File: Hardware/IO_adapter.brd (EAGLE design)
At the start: 67.3 x 41.9 mm, 22 parts, among them Y1 32Khz

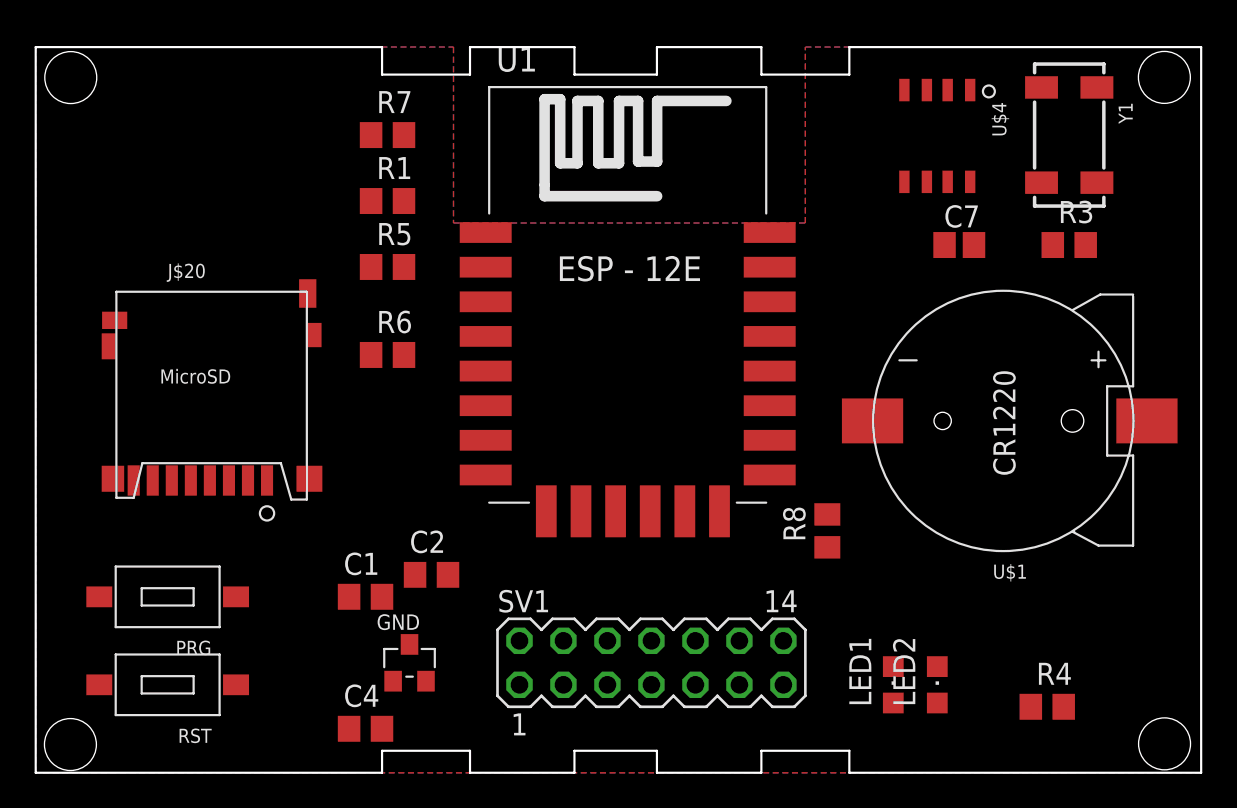
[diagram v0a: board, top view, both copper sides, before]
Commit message: completed routing for both boards
routed out both the base and IO board. Should be ready for verification
There will be errors.
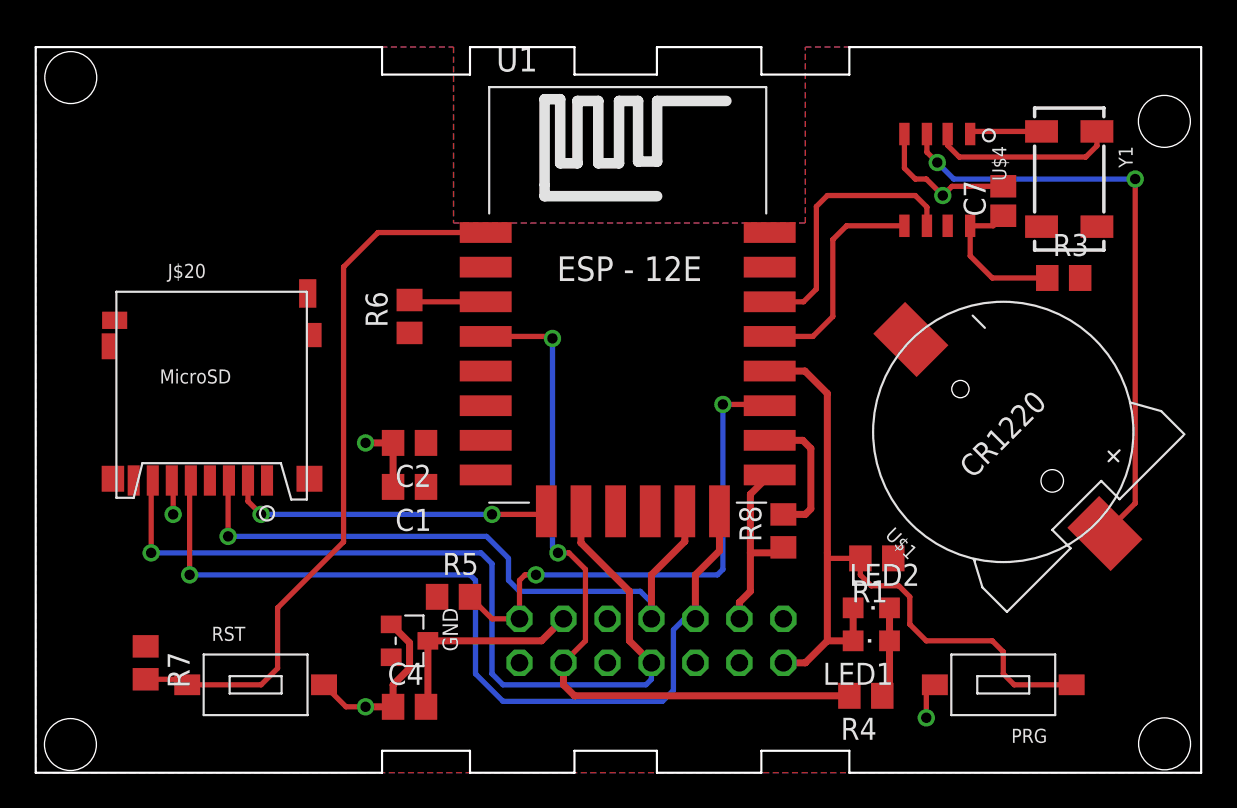
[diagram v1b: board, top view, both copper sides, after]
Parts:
- moved PRG 48.5 mm to (55.9, 5.08)
- moved R1 35.0 mm to (48.6, 12.4), turned to 180 degrees
- moved R7 33.5 mm to (6.35, 6.35), turned to 270 degrees
- moved R5 19.4 mm to (24.1, 10.2)
- moved R4 10.5 mm to (47.9, 4.45), turned to 180 degrees
- moved C2 7.73 mm to (21.6, 19.1), turned to 180 degrees
- moved C1 6.84 mm to (21.6, 16.5), turned to 180 degrees
- moved LED2 5.85 mm to (48.3, 9.53), turned to 270 degrees
- moved RST 5.08 mm to (12.7, 5.08), turned to 0 degrees
- moved C7 3.59 mm to (55.9, 33.0), turned to 90 degrees
- moved LED1 2.84 mm to (48.3, 7.62), turned to 90 degrees
- moved C4 2.84 mm to (21.6, 3.81)
- moved R6 2.56 mm to (21.6, 26.4), turned to 90 degrees
- moved R8 2.54 mm to (43.2, 14.0)
- moved U$4 2.54 mm to (52.1, 34.3)
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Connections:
- removed net ADC10: SV1.2
- removed net GMD: SV1.12
- net 5V: now also SV1.3; no longer SV1.14
- net ADCCS0: now also SV1.1
- net ADCCS1: now also SV1.14; no longer SV1.3
- net CSSD: no longer SV1.10
- net GND: now also SV1.12
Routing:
- net SCLK: track 0.00 -> 51.7 mm, vias 0 -> 1
- net MISO: track 0.00 -> 51.5 mm, vias 0 -> 1
- net ADCCS1: track 0.00 -> 44.3 mm
- net GPIO16: track 0.00 -> 42.4 mm, vias 0 -> 2
- net RST: track 0.00 -> 41.9 mm
- net GND: track 0.00 -> 38.3 mm, vias 0 -> 5
- net MOSI: track 0.00 -> 38.0 mm, vias 0 -> 1
- net VBATT: track 0.00 -> 34.9 mm, vias 0 -> 2
- net ADCCS0: track 0.00 -> 29.9 mm, vias 0 -> 2
- net CSSD: track 0.00 -> 18.8 mm, vias 0 -> 2
- net SCL: track 0.00 -> 15.8 mm
- net SDA: track 0.00 -> 13.0 mm
- net 5V: track 0.00 -> 12.2 mm
- net N$44: track 0.00 -> 10.7 mm
- net N$1: track 0.00 -> 8.87 mm
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
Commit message: added the programming header
I had forgotten the programming header. It's right there now.
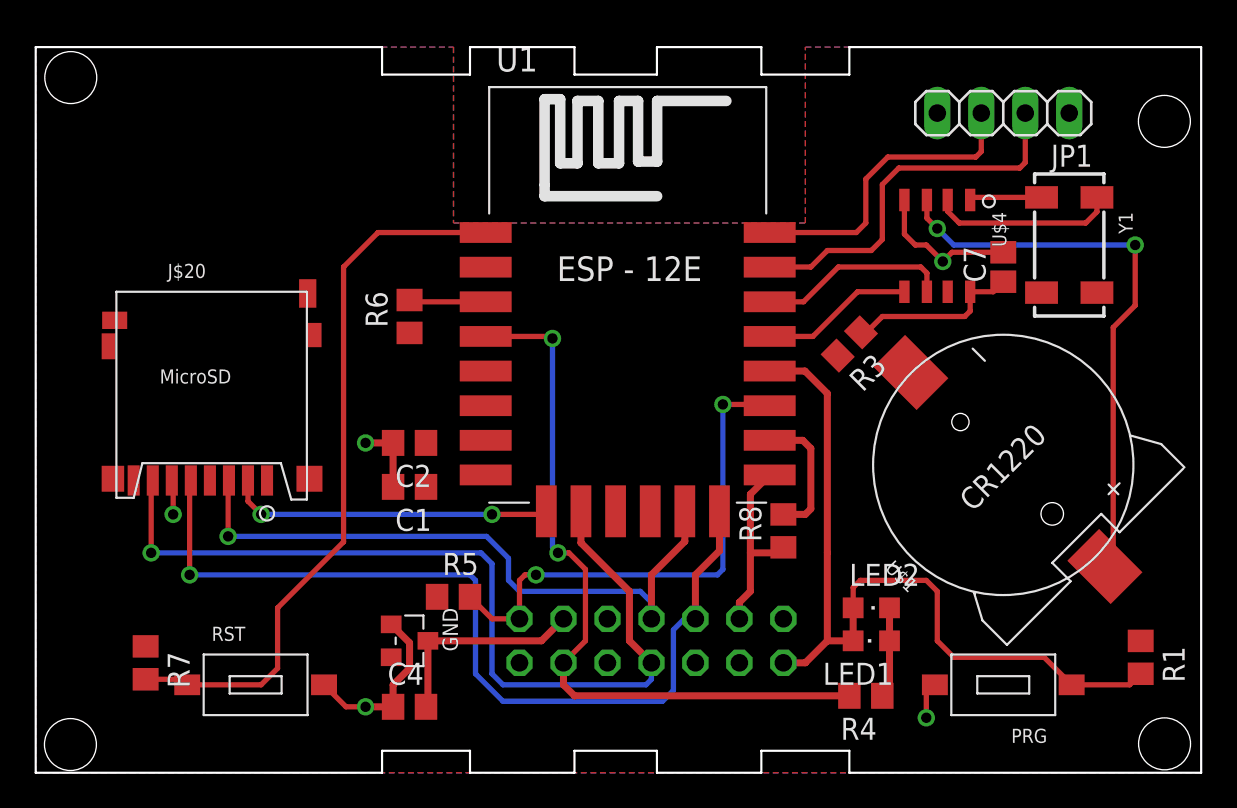
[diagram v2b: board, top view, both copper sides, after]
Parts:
- added JP1: (no value), pinhead:1X04
- moved R1 16.3 mm to (63.8, 6.67), turned to 270 degrees
- moved R3 13.0 mm to (47.0, 24.8), turned to 225 degrees
- moved C7 3.81 mm to (55.9, 29.2)
- moved U$4 3.81 mm to (52.1, 30.5)
- moved Y1 3.81 mm to (59.7, 30.5)
- moved U$1 1.90 mm to (55.9, 17.8)
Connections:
- net 3V3: now also JP1.1
- net GND: now also JP1.4
- net RXD: now also JP1.2
- net TXD: now also JP1.3
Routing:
- net RXD: track 0.00 -> 22.0 mm
- net TXD: track 0.00 -> 17.9 mm
- net SCL: track 15.8 -> 11.1 mm
- net SDA: track 13.0 -> 8.85 mm
- net ADCCS1: track 44.3 -> 47.3 mm
- net VBATT: track 34.9 -> 32.9 mm
- net N$1: track 8.87 -> 10.1 mm

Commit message: moved the MicroSD
now, there is enough room to remove the card in the enclosure
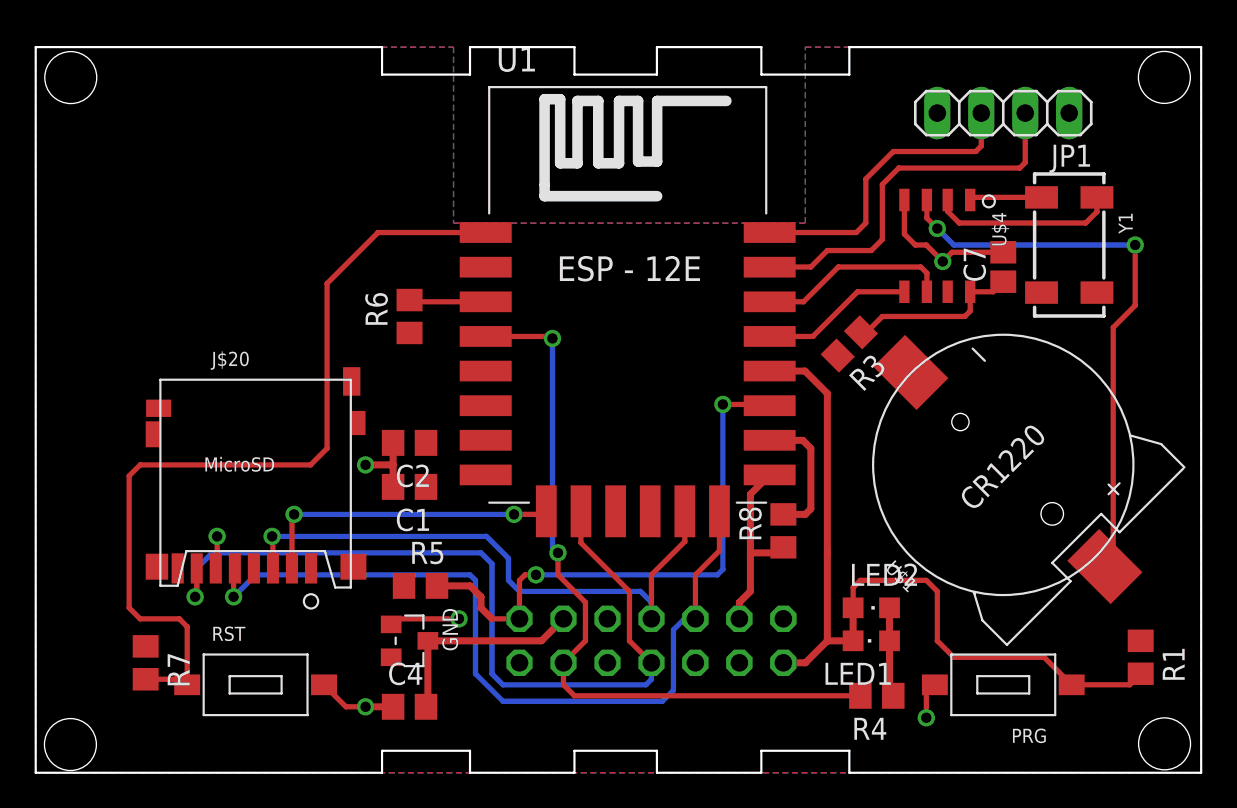
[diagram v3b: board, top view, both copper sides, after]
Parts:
- moved J$20 5.68 mm to (12.7, 12.7)
- moved R5 2.01 mm to (22.2, 10.8)
- moved R4 0.63 mm to (48.6, 4.45)
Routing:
- net RST: track 41.9 -> 49.3 mm
- net SCLK: track 51.7 -> 45.9 mm
- net MOSI: track 38.0 -> 34.1 mm
- net MISO: track 51.5 -> 48.5 mm
- net ADCCS0: track 29.9 -> 32.4 mm
- net GND: track 38.3 -> 36.8 mm, vias 5 -> 6
- net CSSD: track 18.8 -> 17.8 mm
